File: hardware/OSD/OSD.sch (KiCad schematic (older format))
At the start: 35 parts, among them J1 Conn_01x06, J2 Conn_01x05, J3 S, J4 B, J5 B13, J6 W, J7 B1, J8 A5, Q1 MMBT3906, U1 SC662K-3.3V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

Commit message: Add a couple of leds
They could be useful for signaling status and/or errors
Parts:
- added D2, D3: LED, LED_SMD:LED_0603_1608Metric_Pad1.05x0.95mm_HandSolder, symbol Device:LED
- added J9: BOOT0, OSD:PinHeader_SMD_1x01_P1.27mm_Vertical, symbol Connector_Generic:Conn_01x01
- added R12, R13: 100, Resistor_SMD:R_0603_1608Metric_Pad1.05x0.95mm_HandSolder, symbol Device:R
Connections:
- net labels added: BOOT0, LED1, LED2
- wire segments 114 -> 124
- no-connect marks 25 -> 23
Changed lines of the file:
@@
 NoConn ~ 7750 4000
 NoConn ~ 7750 4100
-NoConn ~ 7750 4400
-NoConn ~ 7750 4500
 NoConn ~ 7750 4800
 NoConn ~ 6450 4800
@@
 Text Label 6250 1250 0    50   ~ 0
 PA5
+$Comp
+L Device:LED D2
+U 1 1 5C5E2A8B
+P 10100 4100
+F 0 "D2" H 10092 3845 50  0000 C CNN
+F 1 "LED" H 10092 3936 50  0000 C CNN
+F 2 "LED_SMD:LED_0603_1608Metric_Pad1.05x0.95mm_HandSolder" H 10100 4100 50  0001 C CNN
+F 3 "~" H 10100 4100 50  0001 C CNN
+	1    10100 4100
+	-1   0    0    1
+$EndComp
+$Comp
+L Device:LED D3
+U 1 1 5C5E2ED5
+P 10100 4700
+F 0 "D3" H 10092 4445 50  0000 C CNN
+F 1 "LED" H 10092 4536 50  0000 C CNN
+F 2 "LED_SMD:LED_0603_1608Metric_Pad1.05x0.95mm_HandSolder" H 10100 4700 50  0001 C CNN
+F 3 "~" H 10100 4700 50  0001 C CNN
+	1    10100 4700
+	-1   0    0    1
+$EndComp
+Wire Wire Line
+	10500 4100 10500 4700
+$Comp
+L power:GND #PWR0101
+U 1 1 5C5E795A
+P 10500 5100
+F 0 "#PWR0101" H 10500 4850 50  0001 C CNN
+F 1 "GND" H 10505 4927 50  0000 C CNN
+F 2 "" H 10500 5100 50  0001 C CNN
+F 3 "" H 10500 5100 50  0001 C CNN
+	1    10500 5100
+	1    0    0    -1
+$EndComp
+Wire Wire Line
+	10250 4700 10500 4700
+Connection ~ 10500 4700
+Wire Wire Line
+	10500 4700 10500 5100
+Wire Wire Line
+	10250 4100 10500 4100
+$Comp
+L Device:R R12
+U 1 1 5C5EF8FA
+P 9700 4100
+F 0 "R12" V 9493 4100 50  0000 C CNN
+F 1 "100" V 9584 4100 50  0000 C CNN
+F 2 "Resistor_SMD:R_0603_1608Metric_Pad1.05x0.95mm_HandSolder" V 9630 4100 50  0001 C CNN
+F 3 "~" H 9700 4100 50  0001 C CNN
+	1    9700 4100
+	0    1    1    0
+$EndComp
+$Comp
+L Device:R R13
+U 1 1 5C5EFDB5
+P 9700 4700
+F 0 "R13" V 9493 4700 50  0000 C CNN
+F 1 "100" V 9584 4700 50  0000 C CNN
+F 2 "Resistor_SMD:R_0603_1608Metric_Pad1.05x0.95mm_HandSolder" V 9630 4700 50  0001 C CNN
+F 3 "~" H 9700 4700 50  0001 C CNN
+	1    9700 4700
+	0    1    1    0
+$EndComp
+Wire Wire Line
+	9850 4100 9950 4100
+Wire Wire Line
+	9850 4700 9950 4700
+$Comp
+L Connector_Generic:Conn_01x01 J9
+U 1 1 5C5F9D1F
+P 4550 1600
+F 0 "J9" H 4470 1375 50  0000 C CNN
+F 1 "BOOT0" H 4470 1466 50  0000 C CNN
+F 2 "OSD:PinHeader_SMD_1x01_P1.27mm_Vertical" H 4550 1600 50  0001 C CNN
+F 3 "~" H 4550 1600 50  0001 C CNN
+	1    4550 1600
+	-1   0    0    1
+$EndComp
+Text Label 5350 2400 0    50   ~ 0
+BOOT0
+Text Label 4750 1600 0    50   ~ 0
+BOOT0
+Wire Wire Line
+	9550 4100 9300 4100
+Wire Wire Line
+	9550 4700 9300 4700
+Text Label 9300 4100 0    50   ~ 0
+LED1
+Text Label 9300 4700 0    50   ~ 0
+LED2
+Wire Wire Line
+	7750 4400 8100 4400
+Wire Wire Line
+	7750 4500 8100 4500
+Text Label 8100 4400 0    50   ~ 0
+LED1
+Text Label 8100 4500 0    50   ~ 0
+LED2
 $EndSCHEMATC

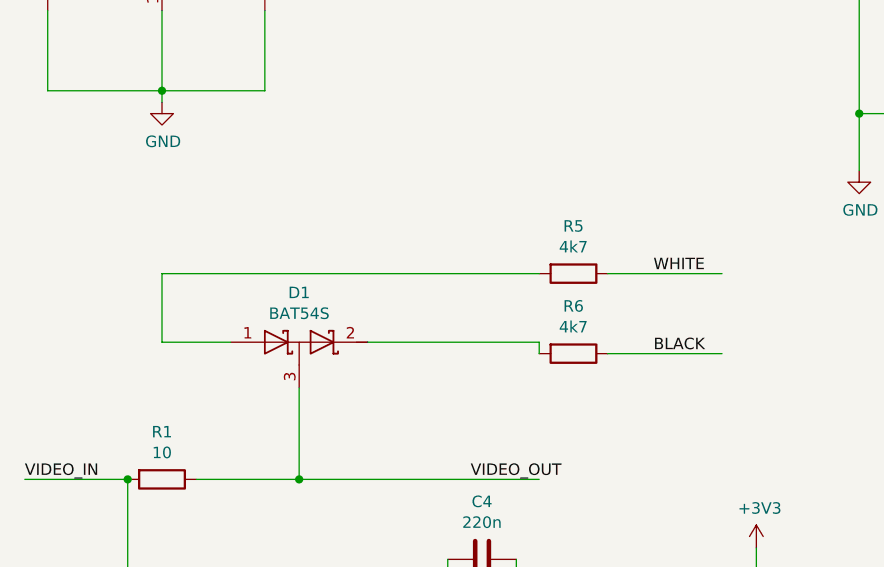
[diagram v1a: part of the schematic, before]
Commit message: Change BLACK and WHITE resistors to 330
4k7 makes the OSD too faint
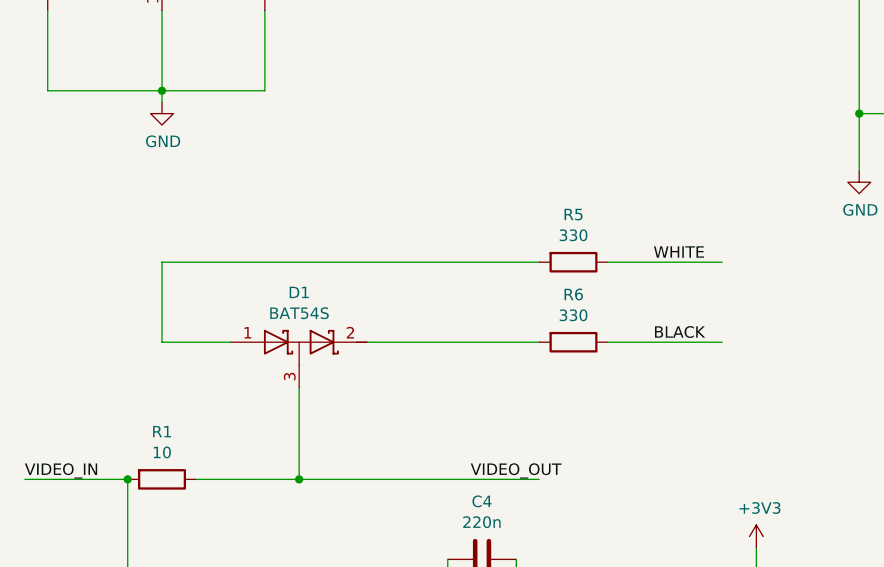
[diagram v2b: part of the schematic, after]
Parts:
- R5, R6: value 4k7 -> 330
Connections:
- wire segments 124 -> 123
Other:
- moved on the sheet: R5, R6
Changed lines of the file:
@@
 L Device:R R5
 U 1 1 5C5C1264
-P 3250 4000
-F 0 "R5" V 3043 4000 50  0000 C CNN
-F 1 "4k7" V 3134 4000 50  0000 C CNN
-F 2 "Resistor_SMD:R_0603_1608Metric_Pad1.05x0.95mm_HandSolder" V 3180 4000 50  0001 C CNN
-F 3 "~" H 3250 4000 50  0001 C CNN
-	1    3250 4000
+P 3250 3950
+F 0 "R5" V 3043 3950 50  0000 C CNN
+F 1 "330" V 3134 3950 50  0000 C CNN
+F 2 "Resistor_SMD:R_0603_1608Metric_Pad1.05x0.95mm_HandSolder" V 3180 3950 50  0001 C CNN
+F 3 "~" H 3250 3950 50  0001 C CNN
+	1    3250 3950
 	0    1    1    0
 $EndComp
@@
 L Device:R R6
 U 1 1 5C5C1323
-P 3250 4350
-F 0 "R6" V 3043 4350 50  0000 C CNN
-F 1 "4k7" V 3134 4350 50  0000 C CNN
-F 2 "Resistor_SMD:R_0603_1608Metric_Pad1.05x0.95mm_HandSolder" V 3180 4350 50  0001 C CNN
-F 3 "~" H 3250 4350 50  0001 C CNN
-	1    3250 4350
+P 3250 4300
+F 0 "R6" V 3043 4300 50  0000 C CNN
+F 1 "330" V 3134 4300 50  0000 C CNN
+F 2 "Resistor_SMD:R_0603_1608Metric_Pad1.05x0.95mm_HandSolder" V 3180 4300 50  0001 C CNN
+F 3 "~" H 3250 4300 50  0001 C CNN
+	1    3250 4300
 	0    1    1    0
 $EndComp
 Wire Wire Line
-	3100 4300 3100 4350
-Wire Wire Line
 	1750 4300 1450 4300
 Wire Wire Line
-	1450 4300 1450 4000
-Wire Wire Line
-	1450 4000 3100 4000
-Wire Wire Line
-	3400 4000 3900 4000
-Wire Wire Line
-	3400 4350 3900 4350
-Text Label 3600 4000 0    50   ~ 0
+	1450 3950 3100 3950
+Wire Wire Line
+	3400 3950 3900 3950
+Wire Wire Line
+	3400 4300 3900 4300
+Text Label 3600 3950 0    50   ~ 0
 WHITE
-Text Label 3600 4350 0    50   ~ 0
+Text Label 3600 4300 0    50   ~ 0
 BLACK
 $Comp
@@
 Text Label 8100 4500 0    50   ~ 0
 LED2
+Wire Wire Line
+	1450 3950 1450 4300
 $EndSCHEMATC
